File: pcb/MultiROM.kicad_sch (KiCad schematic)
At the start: 7 parts, among them J1 Conn_02x22_Row_Letter_First, SW1 SW_DIP_x04, U1 SST39SF010, U2 GAL16V8

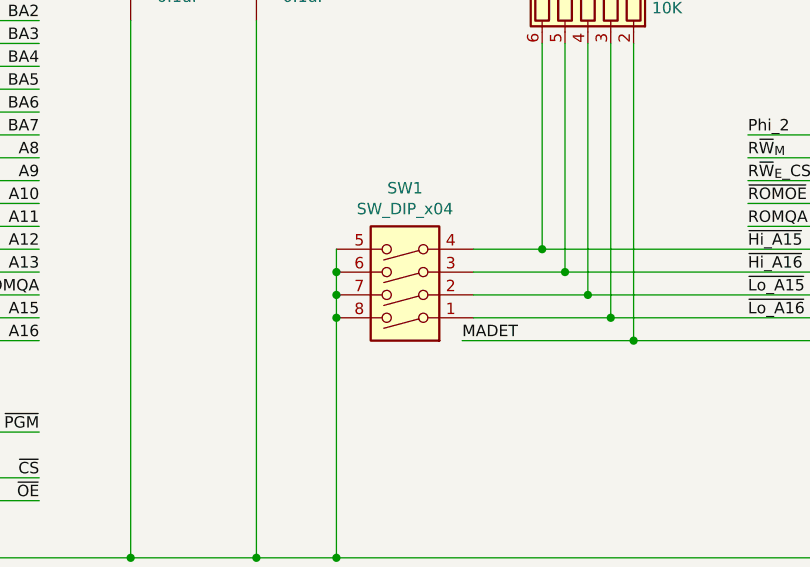
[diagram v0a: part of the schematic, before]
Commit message: Use edge-style DIP switch
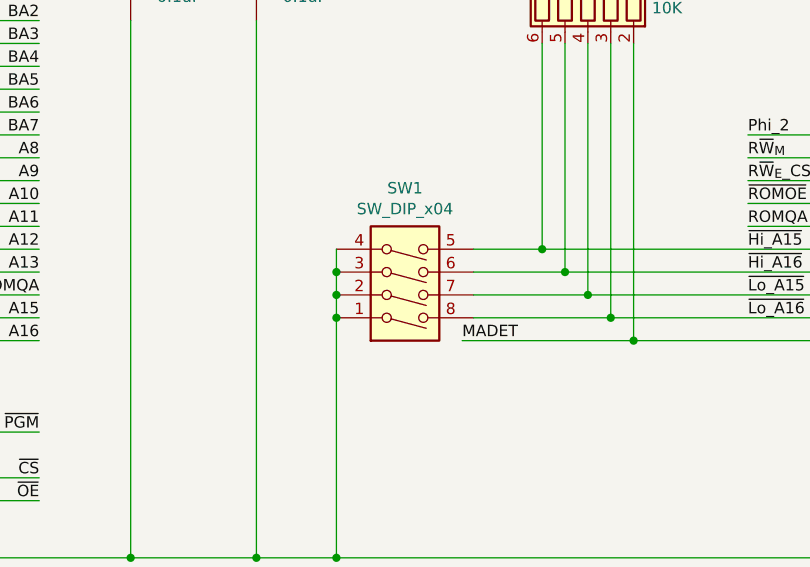
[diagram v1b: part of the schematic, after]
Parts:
- SW1: footprint Button_Switch_THT:SW_DIP_SPSTx04_Slide_9.78x12.34mm_W7.62mm_P2.54mm -> Button_Switch_THT:SW_DIP_SPSTx04_Piano_10.8x11.72mm_W7.62mm_P2.54mm
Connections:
- net GND: now also SW1.1, SW1.2, SW1.3, SW1.4; no longer SW1.5, SW1.6, SW1.7, SW1.8
- net ~{Hi_A15}: now also SW1.5; no longer SW1.4
- net ~{Hi_A16}: now also SW1.6; no longer SW1.3
- net ~{Lo_A15}: now also SW1.7; no longer SW1.2
- net ~{Lo_A16}: now also SW1.8; no longer SW1.1
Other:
- moved on the sheet: SW1
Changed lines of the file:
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@@
     )
   )
-  (symbol (lib_id "Switch:SW_DIP_x04") (at 141.605 120.65 180) (unit 1)
+  (symbol (lib_id "Switch:SW_DIP_x04") (at 141.605 120.65 0) (mirror x) (unit 1)
     (in_bom yes) (on_board yes) (dnp no)
     (property "Reference" "SW1" (at 141.605 111.3282 0)
@@
       (effects (font (size 1.27 1.27)))
     )
-    (property "Footprint" "Button_Switch_THT:SW_DIP_SPSTx04_Slide_9.78x12.34mm_W7.62mm_P2.54mm" (at 141.605 120.65 0)
+    (property "Footprint" "Button_Switch_THT:SW_DIP_SPSTx04_Piano_10.8x11.72mm_W7.62mm_P2.54mm" (at 141.605 120.65 0)
       (effects (font (size 1.27 1.27)) hide)
     )

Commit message: Exclude edge connector from BOM
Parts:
- J1: now left out of the parts list
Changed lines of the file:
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@@
   )
   (symbol (lib_id "Connector_Generic:Conn_02x22_Row_Letter_First") (at 31.75 45.085 0) (unit 1)
-    (in_bom yes) (on_board yes) (dnp no)
+    (in_bom no) (on_board yes) (dnp no)
     (property "Reference" "J1" (at 33.02 14.1732 0)
       (effects (font (size 1.27 1.27)))
